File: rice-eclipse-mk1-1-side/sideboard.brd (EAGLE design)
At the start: 92.4 x 113 mm, 56 parts, among them IC1 MCP6N11R, IC2 MCP6N11R, IC3 LMV321LICTRT, IC4 MCP6N11R, IC5 LMV321LICTRT, IC6 LMV321LICTRT, IC7 MCP6N11R, IC8 LMV321LICTRT

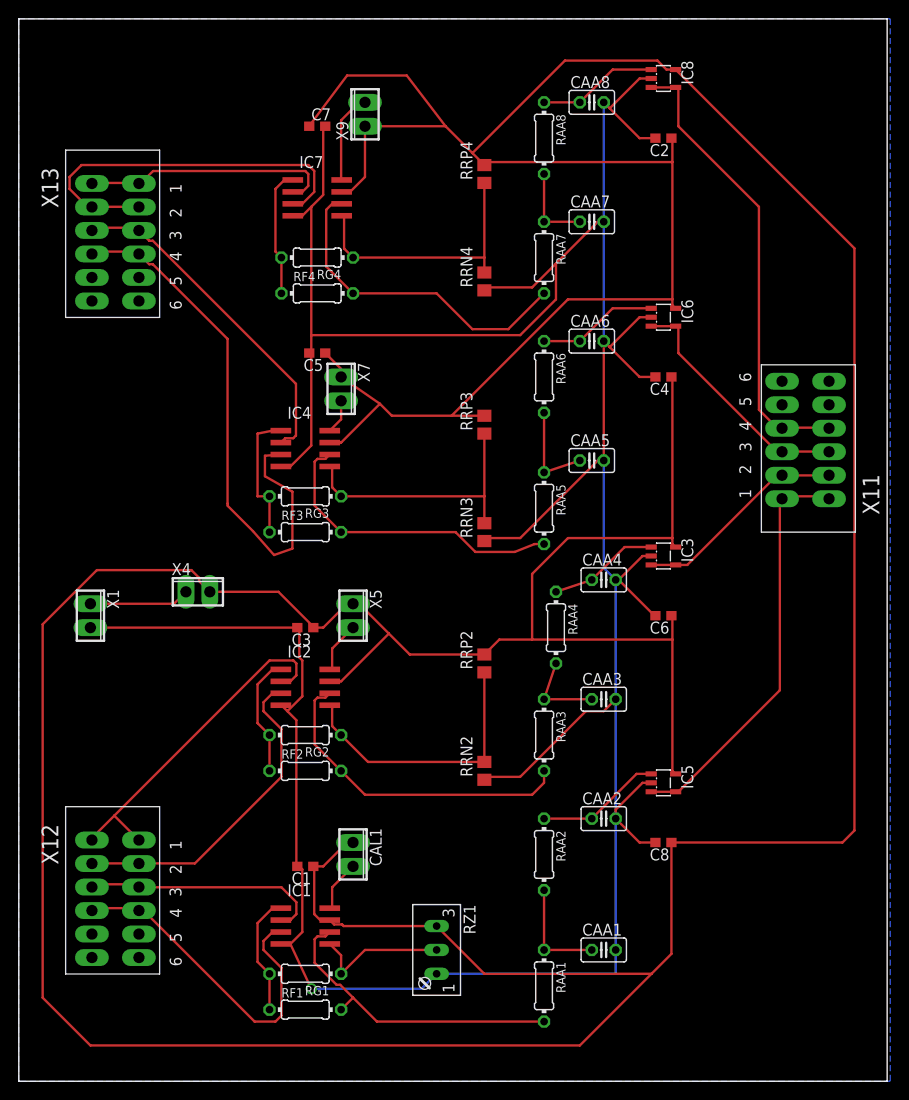
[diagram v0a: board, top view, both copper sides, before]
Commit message: New schematics for Titan amp
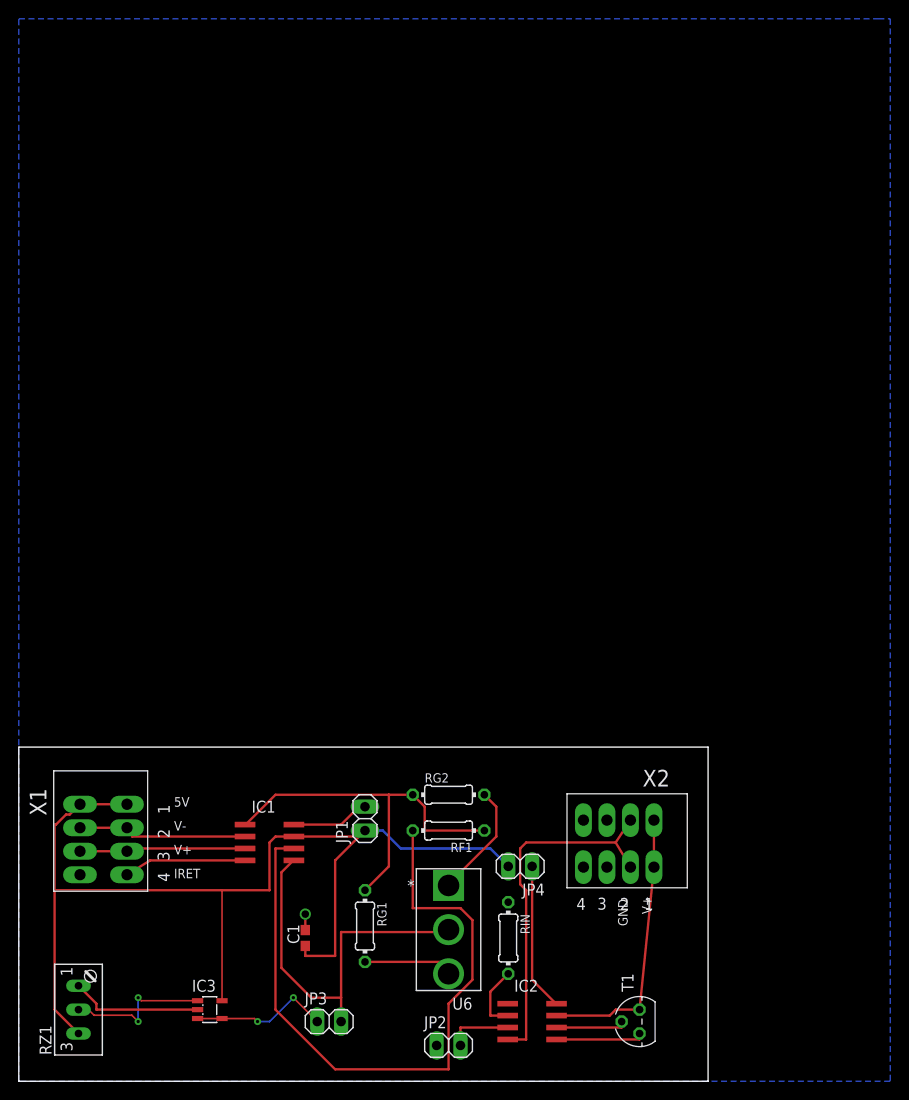
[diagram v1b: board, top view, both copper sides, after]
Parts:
- removed C2, C4, C6, C8: 10nF, rcl:C0603
- removed C3, C5, C7: 1UF, rcl:C0603
- removed CAA1, CAA2, CAA3, CAA4, CAA5, CAA6, CAA7, CAA8: (no value), rcl:C025-025X050
- removed CAL1, X4, X5, X7, X9: (no value), con-phoenix-254:2POL254
- removed IC4, IC7: MCP6N11R, microchip-extra:SO-8
- removed IC5, IC6, IC8: LMV321LICTRT, st-microelectronics-extra:SOT23-5
- removed RAA1, RAA2, RAA3, RAA4, RAA5, RAA6, RAA7, RAA8, RF2, RF3, RF4, RG3, RG4: (no value), rcl:0204/7
- removed RRN2, RRN3, RRN4, RRP2, RRP3, RRP4: (no value), rcl:R0805
- removed X11, X12, X13: (no value), con-phoenix-250-extra:1770924
- added JP1, JP2, JP3, JP4: (no value), pinhead:1X02
- added RIN: 22k, rcl:0204/7
- added T1: 2N3904, transistor-neu-to92:TO92
- added U6: 1101M2S3CQE2, SLIDE_SW:1101M2S3CQE2
- added X2: (no value), con-phoenix-250-extra:1770908
- IC2: value MCP6N11R -> XTR115; device microchip-extra:SO-8 -> texas-extra:SO-8
- X1: device con-phoenix-254:2POL254 -> con-phoenix-250-extra:1770908
- moved IC3 68.2 mm to (20.3, 7.62)
- moved IC2 43.0 mm to (54.6, 6.35)
- moved RZ1 36.1 mm to (7.62, 7.62), turned to 90 degrees
- moved RF1 24.4 mm to (45.7, 26.7), turned to 180 degrees
- moved X1 16.9 mm to (3.81, 33.0)
- moved RG2 16.5 mm to (45.7, 30.5), turned to 0 degrees
- moved IC1 9.67 mm to (26.7, 25.4)
- moved RG1 8.13 mm to (36.8, 16.5), turned to 270 degrees
- moved C1 7.62 mm to (30.5, 15.2), turned to 90 degrees
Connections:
- removed net +3V3: C1.1, C2.1, C3.1, C4.1, C5.1, C6.1, C7.1, C8.1, CAL1.1, IC1.7, IC2.7, IC3.5, IC4.7, IC5.5, IC6.5, IC7.7, IC8.5, RRP2.2, RRP3.2, RRP4.2, RZ1.E, X4.2, X5.1, X7.1, X9.1
- removed net LC1_OUT: IC5.3, IC5.4, X11.P$1, X11.P$7
- removed net LC2_OUT: IC3.3, IC3.4, X11.P$2, X11.P$8
- removed net LC3_OUT: IC6.3, IC6.4, X11.P$3, X11.P$9
- removed net LC4_OUT1: IC8.3, IC8.4, X11.P$10, X11.P$4
- removed net N$12: IC1.3, X12.P$10, X12.P$4
- removed net N$13: IC2.8, X5.2
- removed net N$17: CAA3.1, RAA3.1, RAA4.2
- removed net N$19: IC2.5, RG2.1, RRN2.2, RRP2.1
- removed net N$20: IC7.2, X13.P$1, X13.P$7
- removed net N$21: IC7.3, X13.P$2, X13.P$8
- removed net N$22: IC4.8, X7.2
- removed net N$23: IC4.6, RAA5.2, RF3.2
- removed net N$24: IC4.1, RF3.1, RG3.2
- removed net N$26: CAA5.1, RAA5.1, RAA6.2
- removed net N$27: CAA6.1, IC6.1, RAA6.1
- removed net N$28: IC4.5, RG3.1, RRN3.2, RRP3.1
- removed net N$29: IC4.3, X13.P$10, X13.P$4
- removed net N$30: IC4.2, X13.P$3, X13.P$9
- removed net N$31: IC7.8, X9.2
- removed net N$32: IC7.6, RAA7.2, RF4.2
- removed net N$33: IC7.1, RF4.1, RG4.2
- removed net N$35: CAA7.1, RAA7.1, RAA8.2
- removed net N$36: CAA8.1, IC8.1, RAA8.1
- removed net N$37: IC7.5, RG4.1, RRN4.2, RRP4.1
- new net +5V: C1.1, IC1.7, IC3.5, JP1.1, JP4.2, RZ1.E, X1.P$1, X1.P$5
- new net IRET: C1.2, IC1.4, IC3.2, JP2.1, RIN.1, RZ1.A, X1.P$4, X1.P$8
- new net N$10: IC1.3, X1.P$3, X1.P$7
- new net N$16: IC1.5, JP3.2, U6.2
- new net V+: IC2.7, T1.1, X2.P$1, X2.P$5
- net GND: now also X2.P$2, X2.P$6; no longer C1.2, C2.2, C3.2, C4.2, C5.2, C6.2, C7.2, C8.2, CAA1.2, CAA2.2, CAA3.2, CAA4.2, CAA5.2, CAA6.2, CAA7.2, CAA8.2, IC1.4, IC3.2, IC4.4, IC5.2, IC6.2, IC7.4, IC8.2, RRN2.1, RRN3.1, RRN4.1, RZ1.A, X1.2
- net N$1: now also JP2.2; no longer X12.P$2, X12.P$8
- net N$11: now also X1.P$2, X1.P$6; no longer X12.P$3, X12.P$9
- net N$14: now also RG1.2, U6.3; no longer IC2.6, RAA3.2, RF2.2
- net N$15: now also IC3.1, RZ1.S; no longer IC2.1, RF2.1, RG2.2
- net N$18: now also IC3.3, IC3.4, JP3.1; no longer CAA4.1, IC3.1, RAA4.1
- net N$2: now also RIN.2; no longer X12.P$1, X12.P$7
- net N$3: now also IC2.8, JP4.1; no longer X1.1, X4.1
- net N$4: no longer RAA1.2
- net N$5: now also JP1.2; no longer CAL1.2
- net N$6: now also IC2.5, T1.3; no longer CAA1.1, RAA1.1, RAA2.2
- net N$7: now also RG1.1, RG2.1; no longer RG1.2
- net N$8: now also RG2.2, U6.1; no longer IC1.5, RG1.1, RZ1.S
- net N$9: now also IC2.6, T1.2; no longer CAA2.1, IC5.1, RAA2.1
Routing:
- net +3V3: track 589.6 -> 0.00 mm
- net GND: track 361.7 -> 38.9 mm, vias 1 -> 0
- net +5V: track 0.00 -> 117.1 mm
- net N$29: track 58.8 -> 0.00 mm
- net LC4_OUT1: track 49.3 -> 0.00 mm
- net LC1_OUT: track 44.1 -> 0.00 mm
- net N$21: track 41.6 -> 0.00 mm
- net N$16: track 0.00 -> 40.9 mm
- net N$4: track 34.1 -> 72.2 mm
- net N$12: track 36.8 -> 0.00 mm
- net N$30: track 36.3 -> 0.00 mm
- net N$32: track 35.5 -> 0.00 mm
- net N$23: track 34.1 -> 0.00 mm
- net N$2: track 37.0 -> 7.08 mm
- net N$19: track 29.8 -> 0.00 mm
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- added copper zone on layer 16, net IRET
- removed copper zone on layer 16, net GND
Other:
- board size 92.4 x 113 mm -> 73.3 x 35.5 mm
- board text added: "5V"
- board text added: "GND"
- board text added: "IRET"
- board text added: "V+"
- board text added: "V-"

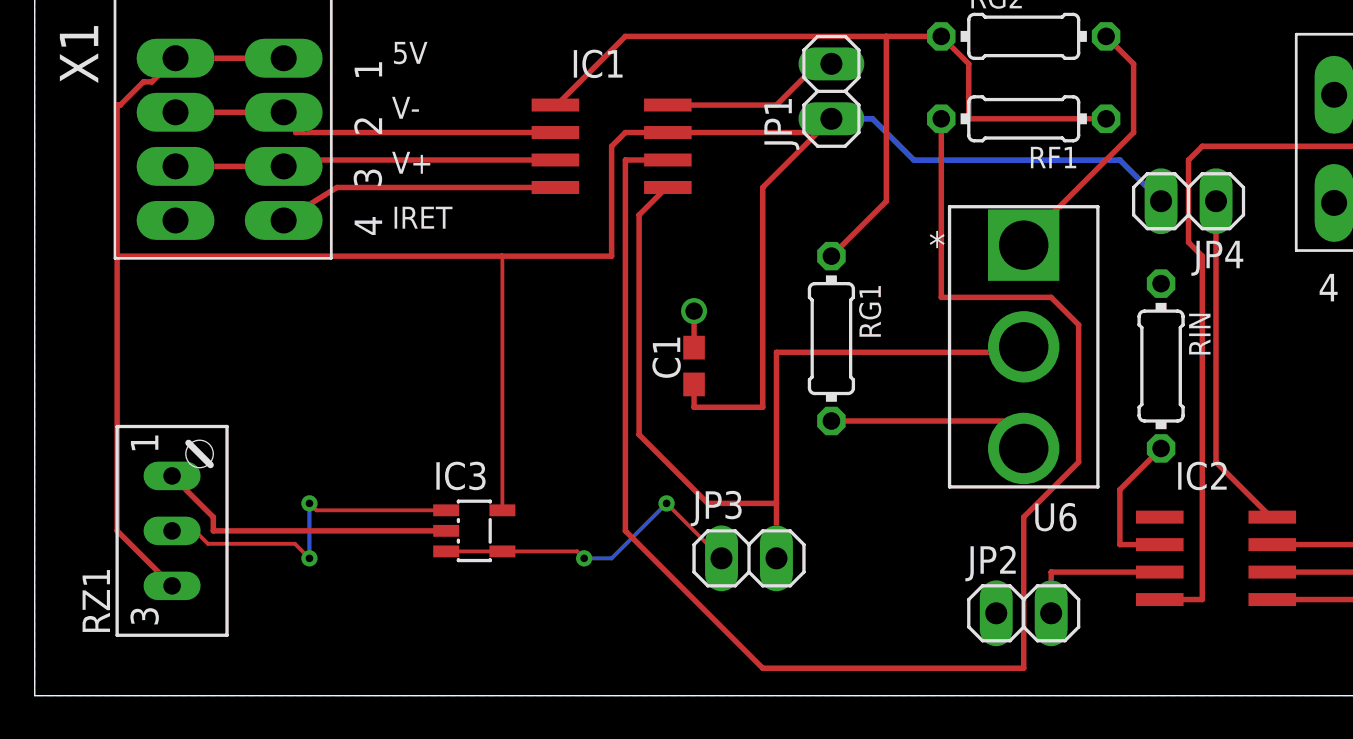
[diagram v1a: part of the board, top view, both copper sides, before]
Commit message: Fixed some routing and minor mistakes with the underlying circuit.
TODO: still want to drill holes in the board.
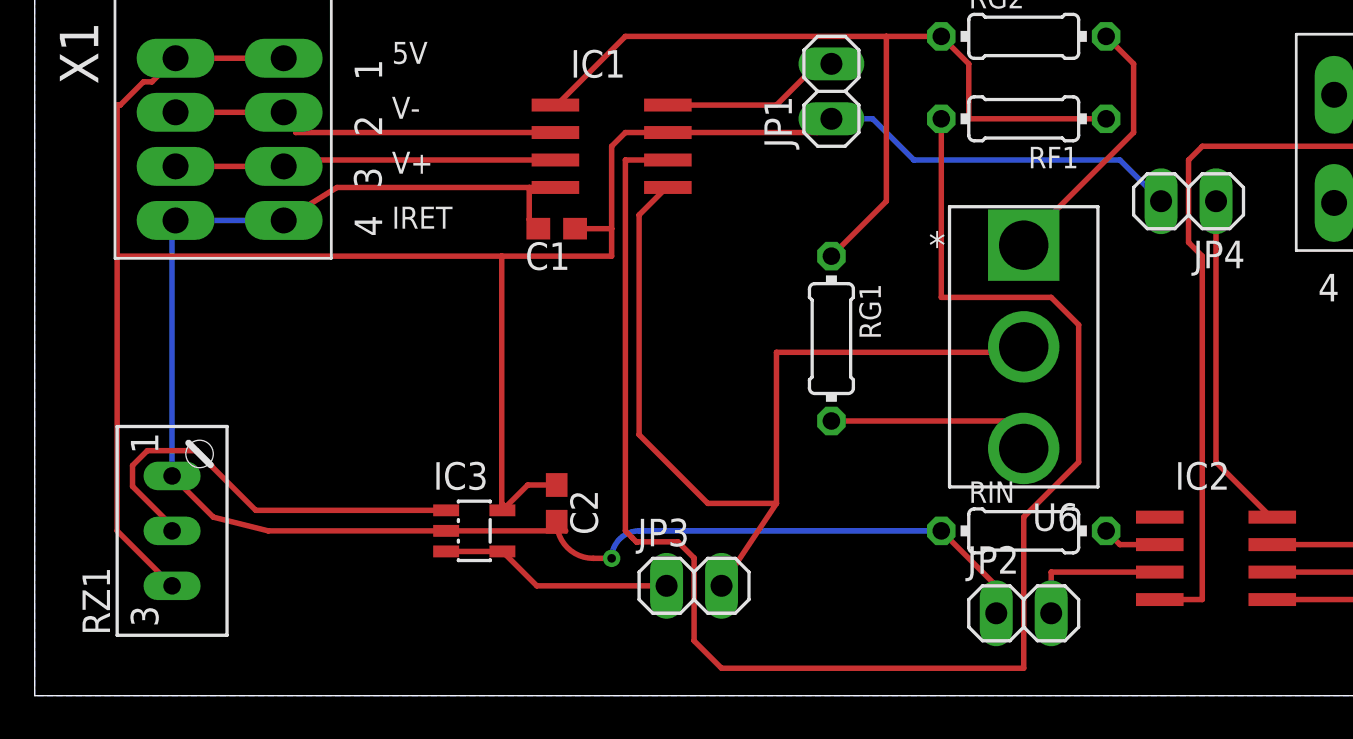
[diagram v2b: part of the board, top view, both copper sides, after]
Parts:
- added C2: 0.1UF, rcl:C0603
- moved RIN 9.92 mm to (45.7, 7.62), turned to 0 degrees
- moved C1 8.98 mm to (24.1, 21.6), turned to 180 degrees
- moved JP3 2.84 mm to (30.5, 5.08)
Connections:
- net +5V: now also C2.1
- net IRET: now also C2.2
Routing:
- net IRET: track 28.8 -> 75.5 mm
- net +5V: track 117.1 -> 103.7 mm
- net N$2: track 7.08 -> 2.74 mm
- net N$15: track 15.9 -> 20.0 mm, vias 2 -> 0
- net N$18: track 15.0 -> 10.8 mm, vias 2 -> 0
- net N$4: track 72.2 -> 74.5 mm
- net N$16: track 40.9 -> 42.9 mm
